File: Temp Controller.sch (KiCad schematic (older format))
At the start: 27 parts, among them J1 Conn_01x03, J2 Conn_02x05_Counter_Clockwise, J3 Conn_01x08, U1 LM317_TO-220, U2 STM32F103CBTx, Y1 16MHz

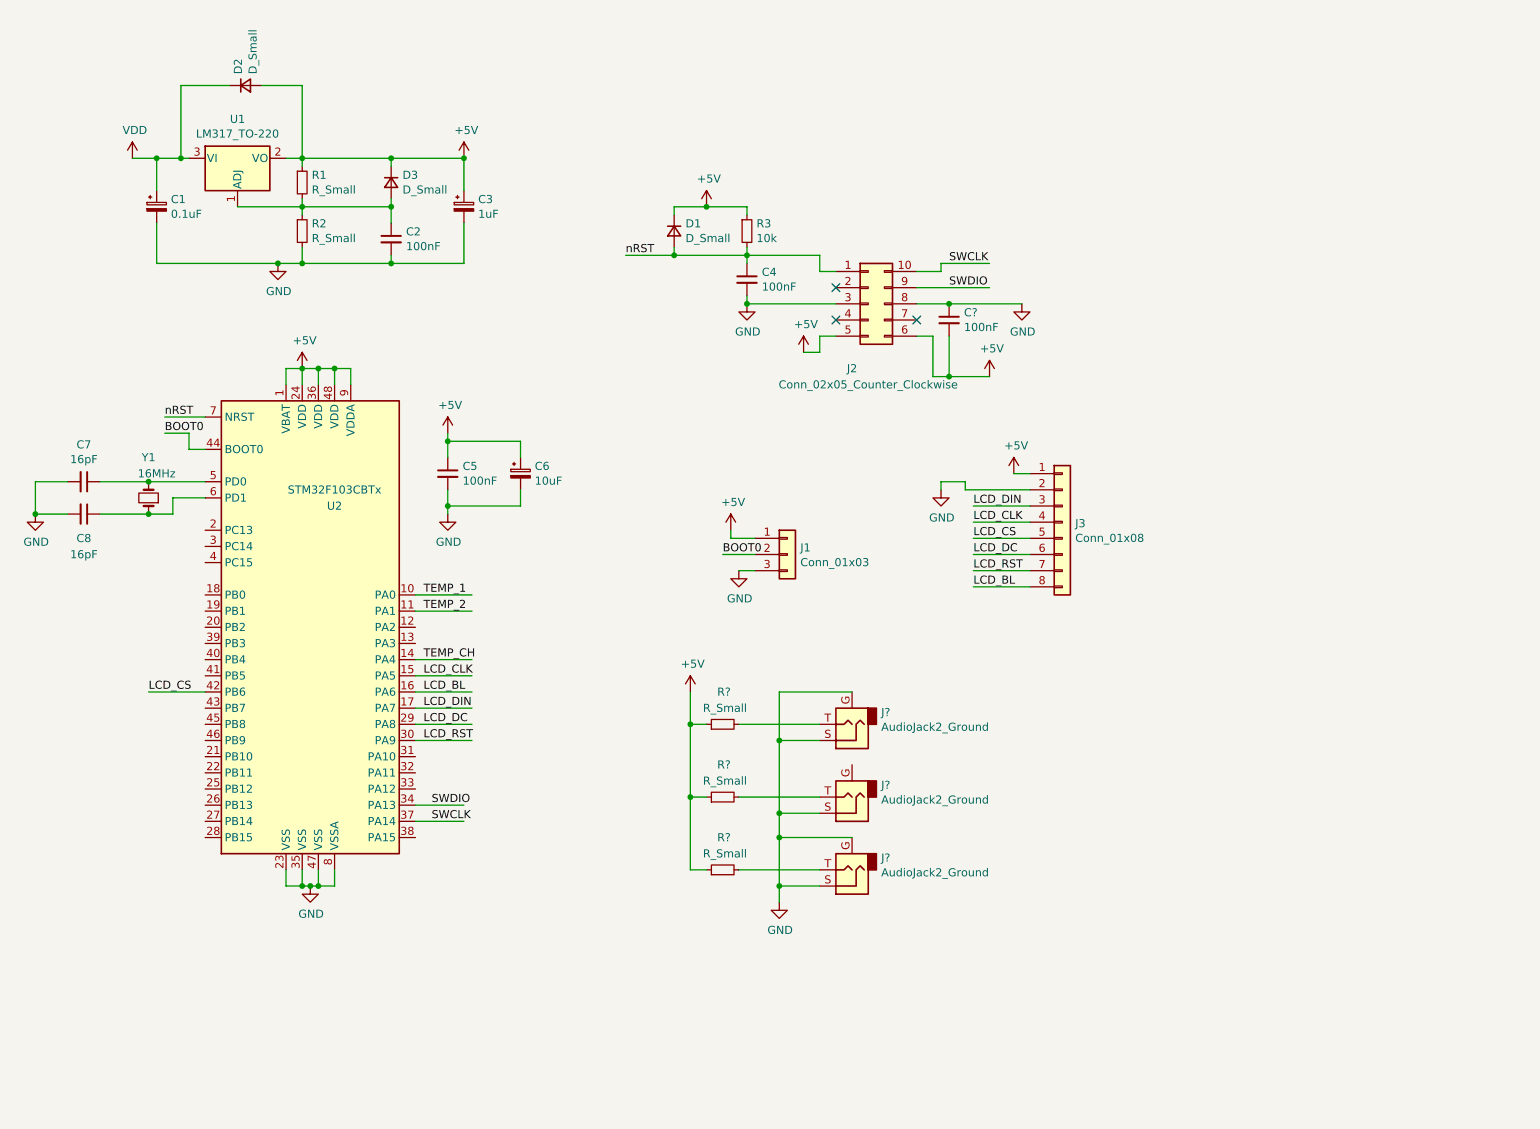
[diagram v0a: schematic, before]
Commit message: -Flipped thermistors for temperature sense -Added filter caps to temperature circuit
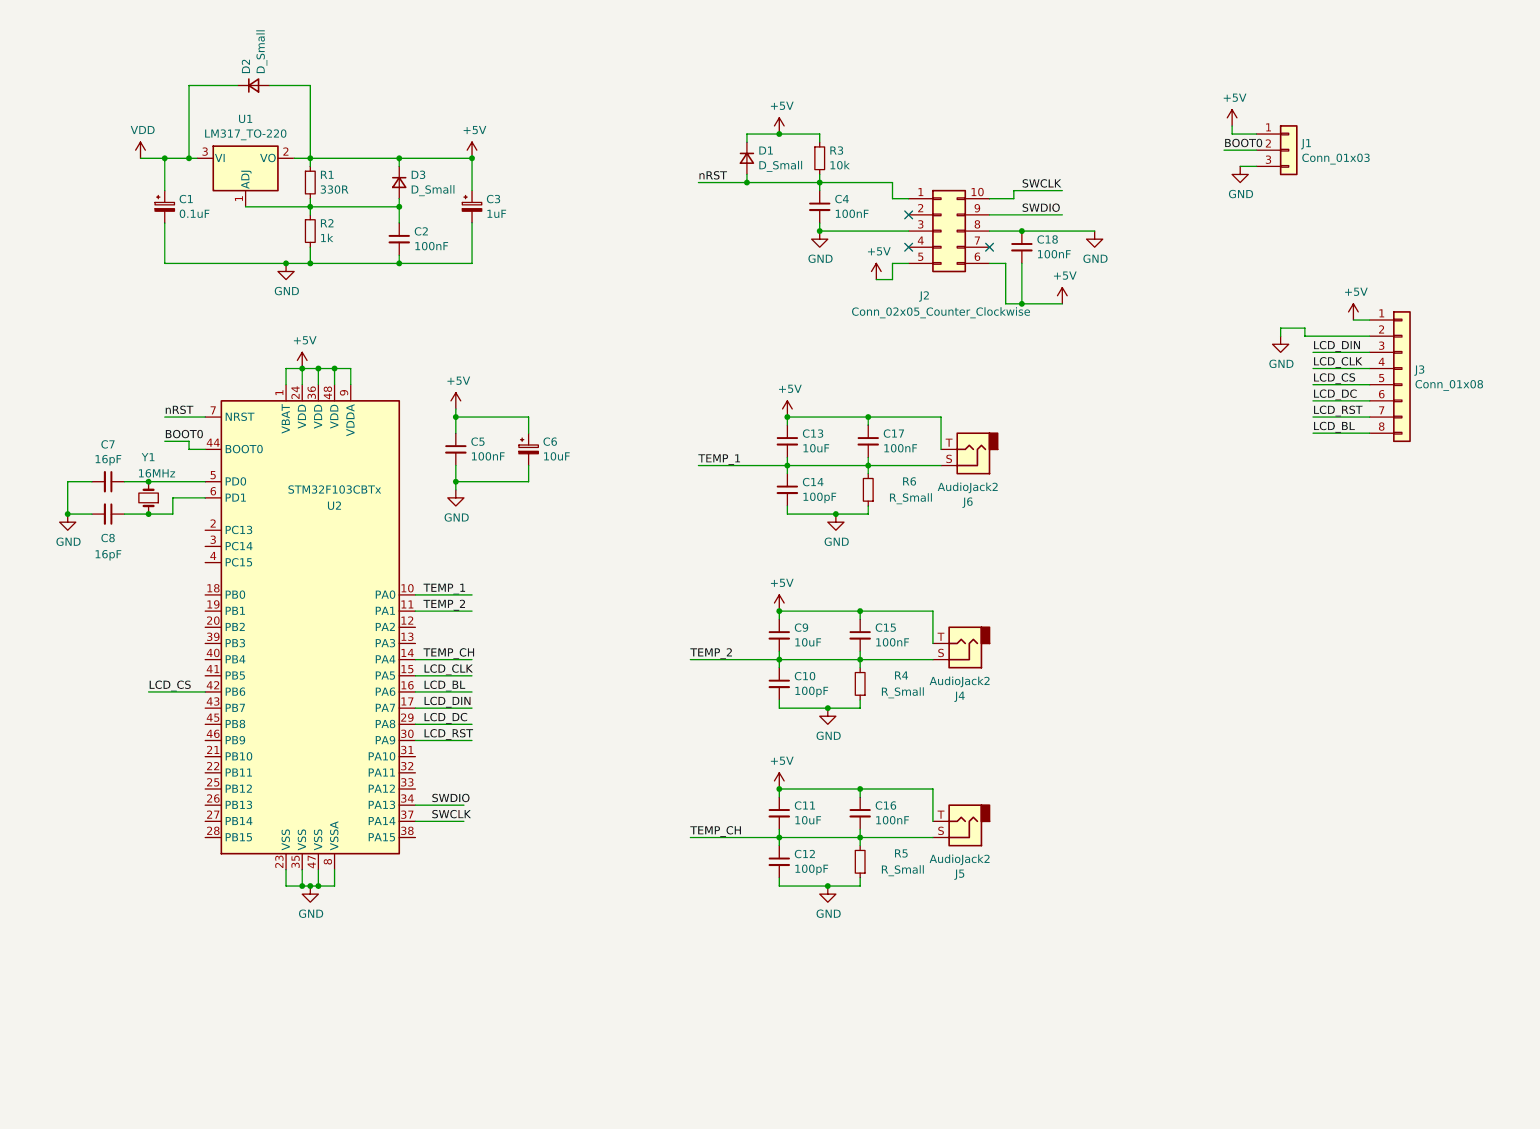
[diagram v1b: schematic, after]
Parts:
- removed J? (x3): AudioJack2_Ground, symbol Connector:AudioJack2_Ground
- removed R? (x2): R_Small, symbol Device:R_Small
- added C10, C12, C14: 100pF, symbol Device:C_Small
- added C11, C13, C9: 10uF, symbol Device:C_Small
- added C15, C16, C17: 100nF, symbol Device:C_Small
- added J4, J5, J6: AudioJack2, symbol Connector:AudioJack2
- added R4, R5: R_Small, symbol Device:R_Small
- R1: value R_Small -> 330R
- R2: value R_Small -> 1k
- gave numbers to parts that had none: 2
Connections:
- wire segments 139 -> 168
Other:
- moved on the sheet: C1, C18, C2, C3, C4, C5, C6, C7, C8, D1, D2, D3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

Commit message: -Fixed debug header pinout -Added current limit resistors for NTC pins -Added reset header -Added USB power input port -Changed LM317 to derive 3.3v supply from 5v
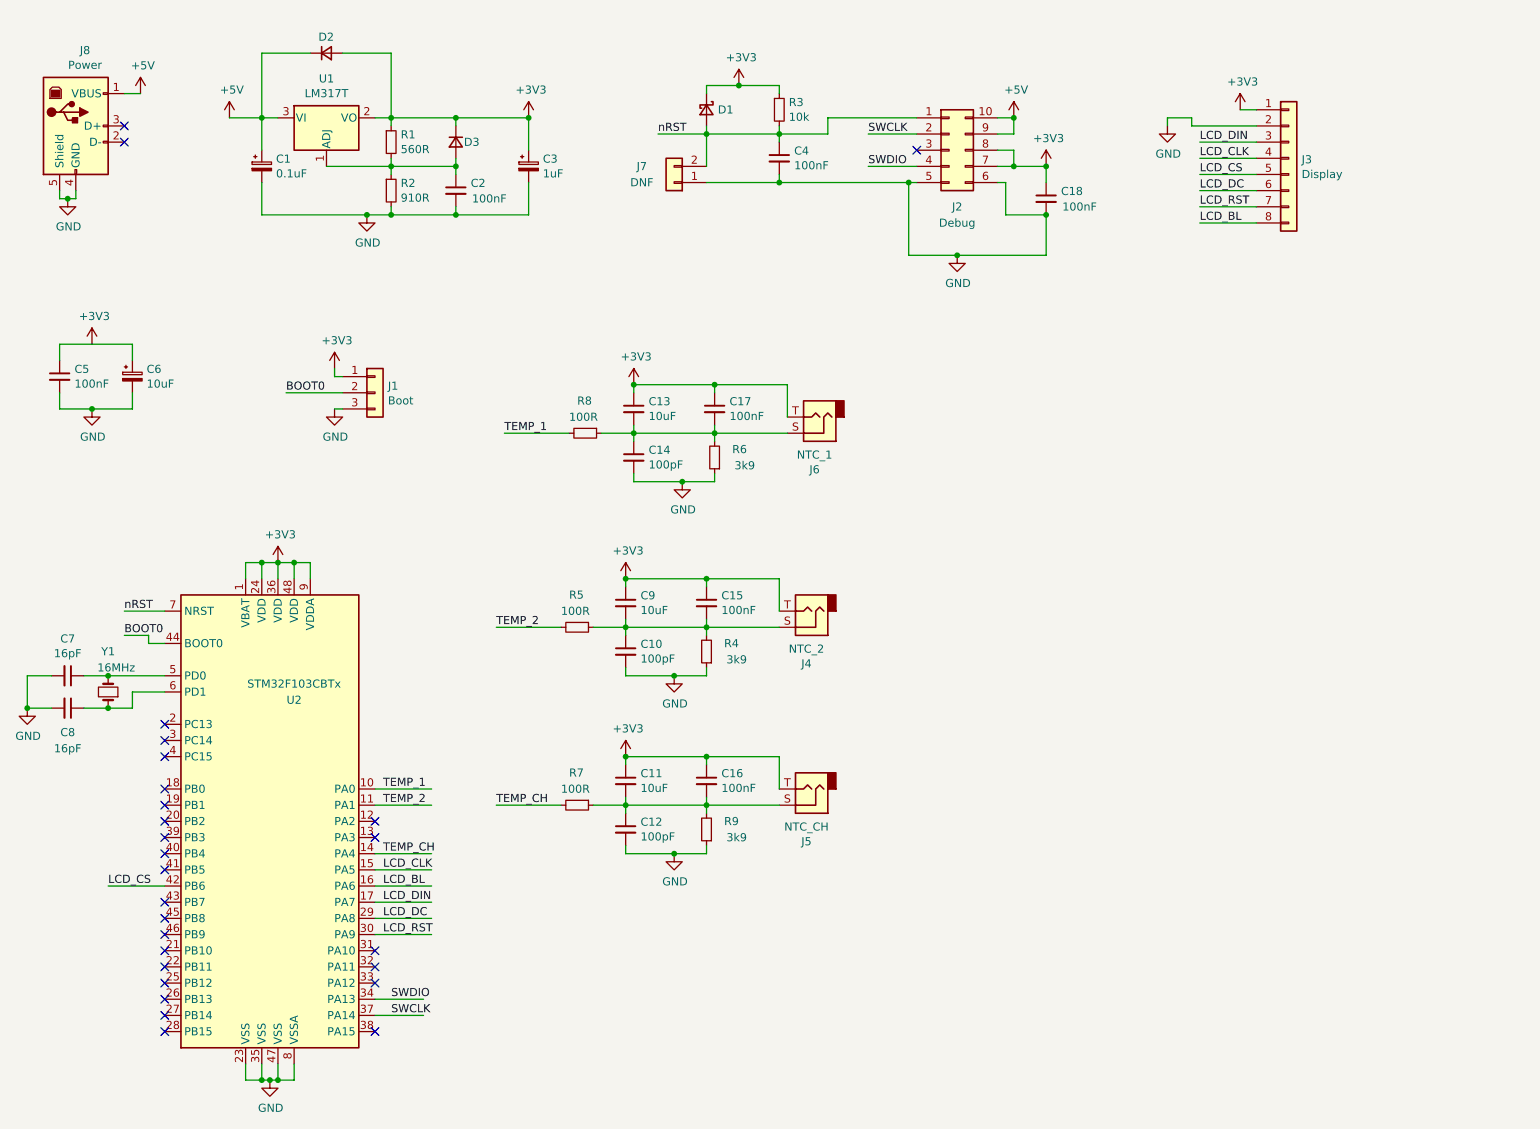
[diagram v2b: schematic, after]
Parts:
- removed D1: D_Small, symbol Device:D_Small
- added D1: D_Schottky_Small, symbol Device:D_Schottky_Small
- added J7: DNF, symbol Connector_Generic:Conn_01x02
- added J8: Power, symbol Connector:USB_B
- added R7, R8: 100R, symbol Device:R_Small
- added R9: 3k9, symbol Device:R_Small
- J1: value Conn_01x03 -> Boot
- J2: value Conn_02x05_Counter_Clockwise -> Debug
- J3: value Conn_01x08 -> Display
- J4: value AudioJack2 -> NTC_2
- J5: value AudioJack2 -> NTC_CH
- J6: value AudioJack2 -> NTC_1
- R1: value 330R -> 560R
- R2: value 1k -> 910R
- R4, R6: value R_Small -> 3k9
- R5: value R_Small -> 100R
- U1: value LM317_TO-220 -> LM317T
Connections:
- net labels added: +3V3
- net labels removed: VDD
- wire segments 168 -> 180
- no-connect marks 3 -> 27
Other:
- moved on the sheet: C1, C10, C11, C12, C13, C14, C15, C16, C17, C2, C3, C4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

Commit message: -Fixed micro pin connections from LCD -Added standby LED
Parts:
- added D4: LED_STBY, LED_SMD:LED_Avago_PLCC4_3.2x2.8mm_CW, symbol LED:ASMB-MTB0-0A3A2
- added J9: USART2, symbol Connector_Generic:Conn_01x02
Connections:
- net labels added: LED_B, LED_G, LED_R, USART2_RX, USART2_TX, USB_DM, USB_DP
- wire segments 180 -> 195
- no-connect marks 27 -> 18
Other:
- moved on the sheet: J1
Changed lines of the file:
@@
 Text Label 5950 1450 0    50   ~ 0
 SWDIO
-Text Label 3000 6600 0    50   ~ 0
+Text Label 3100 6600 0    50   ~ 0
 SWDIO
-Text Label 3000 6700 0    50   ~ 0
+Text Label 3100 6700 0    50   ~ 0
 SWCLK
-Wire Wire Line
-	2900 6700 3200 6700
-Wire Wire Line
-	2900 6600 3200 6600
 $Comp
 L Device:Crystal_Small Y1
@@
 L Connector_Generic:Conn_01x03 J1
 U 1 1 6271A159
-P 2900 2850
-F 0 "J1" H 2980 2892 50  0000 L CNN
-F 1 "Boot" H 2980 2801 50  0000 L CNN
-F 2 "" H 2900 2850 50  0001 C CNN
-F 3 "~" H 2900 2850 50  0001 C CNN
-	1    2900 2850
+P 2700 2800
+F 0 "J1" H 2780 2842 50  0000 L CNN
+F 1 "Boot" H 2780 2751 50  0000 L CNN
+F 2 "" H 2700 2800 50  0001 C CNN
+F 3 "~" H 2700 2800 50  0001 C CNN
+	1    2700 2800
 	1    0    0    -1
 $EndComp
@@
 Text Label 1350 4350 0    50   ~ 0
 BOOT0
-Text Label 2350 2850 0    50   ~ 0
+Text Label 2150 2800 0    50   ~ 0
 BOOT0
 $Comp
 L power:GND #PWR012
 U 1 1 627360EA
-P 2650 2950
-F 0 "#PWR012" H 2650 2700 50  0001 C CNN
-F 1 "GND" H 2655 2777 50  0000 C CNN
-F 2 "" H 2650 2950 50  0001 C CNN
-F 3 "" H 2650 2950 50  0001 C CNN
-	1    2650 2950
-	1    0    0    -1
-$EndComp
-Wire Wire Line
-	2700 2950 2650 2950
-Wire Wire Line
-	2650 2750 2650 2700
+P 2450 2900
+F 0 "#PWR012" H 2450 2650 50  0001 C CNN
+F 1 "GND" H 2455 2727 50  0000 C CNN
+F 2 "" H 2450 2900 50  0001 C CNN
+F 3 "" H 2450 2900 50  0001 C CNN
+	1    2450 2900
+	1    0    0    -1
+$EndComp
+Wire Wire Line
+	2500 2900 2450 2900
+Wire Wire Line
+	2450 2700 2450 2650
 $Comp
 L Connector_Generic:Conn_01x08 J3
@@
 Wire Wire Line
 	2250 7100 2300 7100
-Text Label 1250 5900 0    50   ~ 0
+Text Label 1150 5900 0    50   ~ 0
 LCD_CS
-Wire Wire Line
-	1600 5900 1250 5900
-Text Label 2950 6000 0    50   ~ 0
+Text Label 1150 5800 0    50   ~ 0
 LCD_DIN
-Text Label 2950 5800 0    50   ~ 0
+Text Label 1150 5600 0    50   ~ 0
 LCD_CLK
-Text Label 2950 5900 0    50   ~ 0
+Text Label 3050 5900 0    50   ~ 0
 LCD_BL
-Text Label 2950 6100 0    50   ~ 0
+Text Label 3050 6100 0    50   ~ 0
 LCD_DC
-Text Label 2950 6200 0    50   ~ 0
+Text Label 3050 6200 0    50   ~ 0
 LCD_RST
-Wire Wire Line
-	2900 6200 3250 6200
-Wire Wire Line
-	2900 6100 3250 6100
-Wire Wire Line
-	2900 6000 3250 6000
-Wire Wire Line
-	2900 5900 3250 5900
-Wire Wire Line
-	2900 5800 3250 5800
-Wire Wire Line
-	2900 5700 3250 5700
-Text Label 2950 5700 0    50   ~ 0
+Text Label 3000 5700 0    50   ~ 0
 TEMP_CH
 $Comp
@@
 	2850 1750 3000 1750
 Wire Wire Line
-	2350 2850 2700 2850
+	2150 2800 2500 2800
 $Comp
 L Connector_Generic:Conn_01x02 J7
@@
 	1050 1650 1050 1600
 Connection ~ 1000 1650
-NoConn ~ 1350 1200
-NoConn ~ 1350 1300
 $Comp
 L power:+3V3 #PWR0109
@@
 L power:+3V3 #PWR0110
 U 1 1 62CB1D58
-P 2650 2700
-F 0 "#PWR0110" H 2650 2550 50  0001 C CNN
-F 1 "+3V3" H 2665 2873 50  0000 C CNN
-F 2 "" H 2650 2700 50  0001 C CNN
-F 3 "" H 2650 2700 50  0001 C CNN
-	1    2650 2700
-	1    0    0    -1
-$EndComp
-Wire Wire Line
-	2650 2750 2700 2750
+P 2450 2650
+F 0 "#PWR0110" H 2450 2500 50  0001 C CNN
+F 1 "+3V3" H 2465 2823 50  0000 C CNN
+F 2 "" H 2450 2650 50  0001 C CNN
+F 3 "" H 2450 2650 50  0001 C CNN
+	1    2450 2650
+	1    0    0    -1
+$EndComp
+Wire Wire Line
+	2450 2700 2500 2700
 Connection ~ 1150 2950
 Wire Wire Line
@@
 	0    1    1    0
 $EndComp
-Wire Wire Line
-	2900 5400 3250 5400
-Text Label 2950 5400 0    50   ~ 0
+Text Label 3050 5400 0    50   ~ 0
 TEMP_2
-Wire Wire Line
-	2900 5300 3250 5300
-Text Label 2950 5300 0    50   ~ 0
+Text Label 3050 5300 0    50   ~ 0
 TEMP_1
 Wire Wire Line
@@
 	-1   0    0    1
 $EndComp
-NoConn ~ 1600 4900
-NoConn ~ 1600 5000
-NoConn ~ 1600 5100
-NoConn ~ 1600 5300
-NoConn ~ 1600 5400
+Text Label 2950 5500 0    50   ~ 0
+USART2_TX
+Text Label 2950 5600 0    50   ~ 0
+USART2_RX
+Wire Wire Line
+	2900 5600 3350 5600
+Wire Wire Line
+	2900 5500 3350 5500
+Wire Wire Line
+	2900 5400 3350 5400
+Wire Wire Line
+	2900 5300 3350 5300
+Wire Wire Line
+	2900 5700 3350 5700
+Wire Wire Line
+	1150 5600 1600 5600
+Wire Wire Line
+	2900 5900 3350 5900
+Wire Wire Line
+	2900 6100 3350 6100
+Wire Wire Line
+	2900 6200 3350 6200
+Wire Wire Line
+	2900 6600 3350 6600
+Wire Wire Line
+	2900 6700 3350 6700
+$Comp
+L Connector_Generic:Conn_01x02 J9
+U 1 1 631670E7
+P 9300 1500
+F 0 "J9" H 9218 1175 50  0000 C CNN
+F 1 "USART2" H 9218 1266 50  0000 C CNN
+F 2 "" H 9300 1500 50  0001 C CNN
+F 3 "~" H 9300 1500 50  0001 C CNN
+	1    9300 1500
+	-1   0    0    1
+$EndComp
+Text Label 9550 1400 0    50   ~ 0
+USART2_TX
+Text Label 9550 1500 0    50   ~ 0
+USART2_RX
+Wire Wire Line
+	9500 1500 9950 1500
+Wire Wire Line
+	9500 1400 9950 1400
+NoConn ~ 2900 5800
+Wire Wire Line
+	1150 5800 1600 5800
+Wire Wire Line
+	2900 6000 3350 6000
+Text Label 3100 6000 0    50   ~ 0
+LED_R
+Wire Wire Line
+	1150 5300 1600 5300
+Wire Wire Line
+	1150 5400 1600 5400
+Text Label 1150 5300 0    50   ~ 0
+LED_G
+Text Label 1150 5400 0    50   ~ 0
+LED_B
+Wire Wire Line
+	1150 5900 1600 5900
 NoConn ~ 1600 5500
-NoConn ~ 1600 5600
-NoConn ~ 1600 5700
-NoConn ~ 1600 5800
-NoConn ~ 1600 6000
-NoConn ~ 1600 6100
-NoConn ~ 1600 6200
 NoConn ~ 1600 6300
 NoConn ~ 1600 6400
@@
 NoConn ~ 1600 6700
 NoConn ~ 1600 6800
+NoConn ~ 2900 6300
+Text Label 1350 1200 0    50   ~ 0
+USB_DP
+Text Label 1350 1300 0    50   ~ 0
+USB_DM
+Wire Wire Line
+	1350 1300 1650 1300
+Wire Wire Line
+	1350 1200 1650 1200
+Text Label 3050 6500 0    50   ~ 0
+USB_DP
+Text Label 3050 6400 0    50   ~ 0
+USB_DM
+Wire Wire Line
+	2900 6400 3350 6400
+Wire Wire Line
+	2900 6500 3350 6500
 NoConn ~ 2900 6800
-NoConn ~ 2900 6500
-NoConn ~ 2900 6400
-NoConn ~ 2900 6300
-NoConn ~ 2900 5600
-NoConn ~ 2900 5500
+NoConn ~ 1600 5700
+NoConn ~ 1600 6000
+NoConn ~ 1600 6100
+NoConn ~ 1600 6200
+$Comp
+L LED:ASMB-MTB0-0A3A2 D4
+U 1 1 633BC01E
+P 6600 3000
+F 0 "D4" H 6600 2483 50  0000 C CNN
+F 1 "LED_STBY" H 6600 2574 50  0000 C CNN
+F 2 "LED_SMD:LED_Avago_PLCC4_3.2x2.8mm_CW" H 6600 3500 50  0001 C CNN
+F 3 "https://docs.broadcom.com/docs/AV02-4186EN" H 6600 2550 50  0001 C CNN
+	1    6600 3000
+	-1   0    0    1
+$EndComp
+$Comp
+L power:+3V3 #PWR01
+U 1 1 633C2CEE
+P 6350 3000
+F 0 "#PWR01" H 6350 2850 50  0001 C CNN
+F 1 "+3V3" H 6365 3173 50  0000 C CNN
+F 2 "" H 6350 3000 50  0001 C CNN
+F 3 "" H 6350 3000 50  0001 C CNN
+	1    6350 3000
+	1    0    0    -1
+$EndComp
+Wire Wire Line
+	6400 3000 6350 3000
+Text Label 6950 3000 0    50   ~ 0
+LED_G
+Text Label 6950 2800 0    50   ~ 0
+LED_B
+Text Label 6950 3200 0    50   ~ 0
+LED_R
+Wire Wire Line
+	6800 2800 7200 2800
+Wire Wire Line
+	6800 3000 7200 3000
+Wire Wire Line
+	6800 3200 7200 3200
+NoConn ~ 1600 4900
+NoConn ~ 1600 5000
+NoConn ~ 1600 5100
 $EndSCHEMATC
